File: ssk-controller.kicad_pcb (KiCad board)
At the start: 2 copper layers, 170 x 50 mm, 34 parts, among them J1 Conn_01x16, J2 Conn_01x08, J3 Conn_01x01, J4 USB_B, J5 Solenoid, J6 Solenoid_Signal, Q1 Q_NMOS_GSD, SW1 SW_Push, U1 ATmega32U4-AU, U2 PRTR5V0U2X, Y1 16Mhz

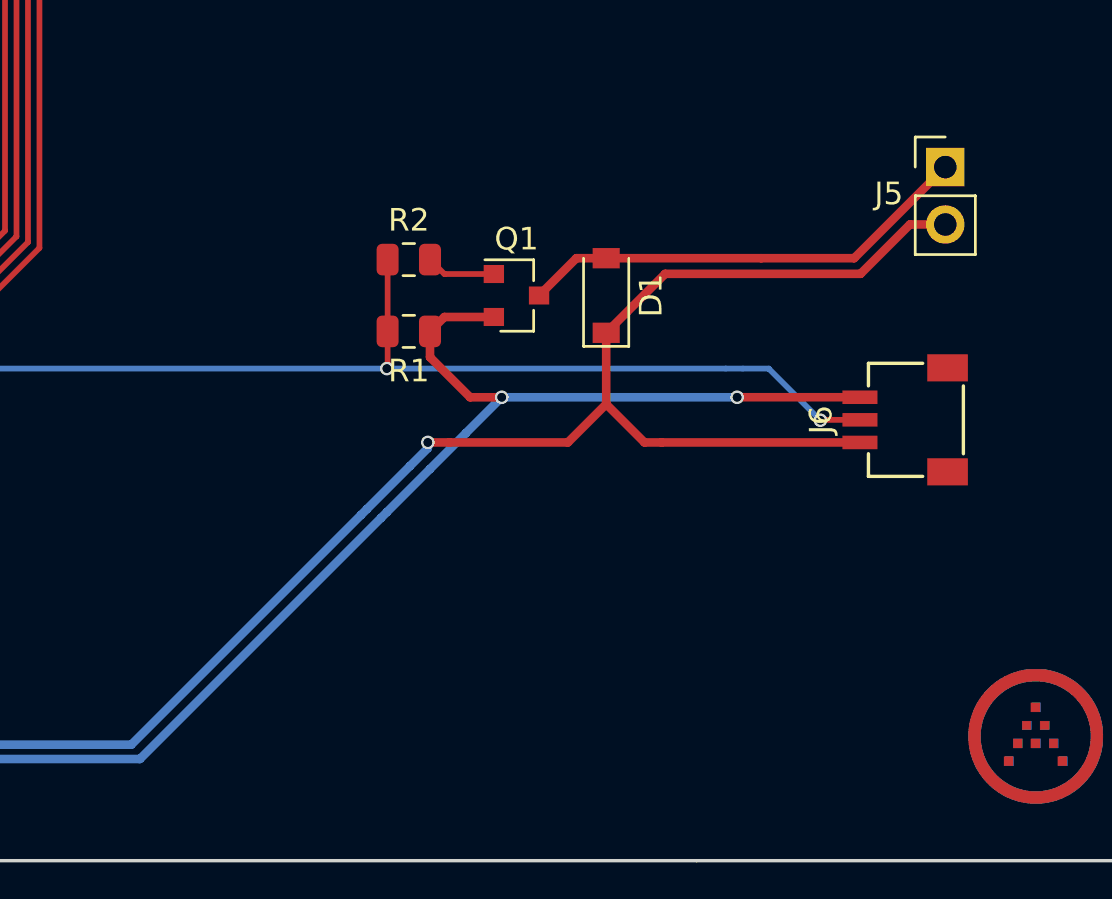
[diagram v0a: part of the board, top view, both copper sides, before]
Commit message: Remove JST header, focus on 5V direct solenoid
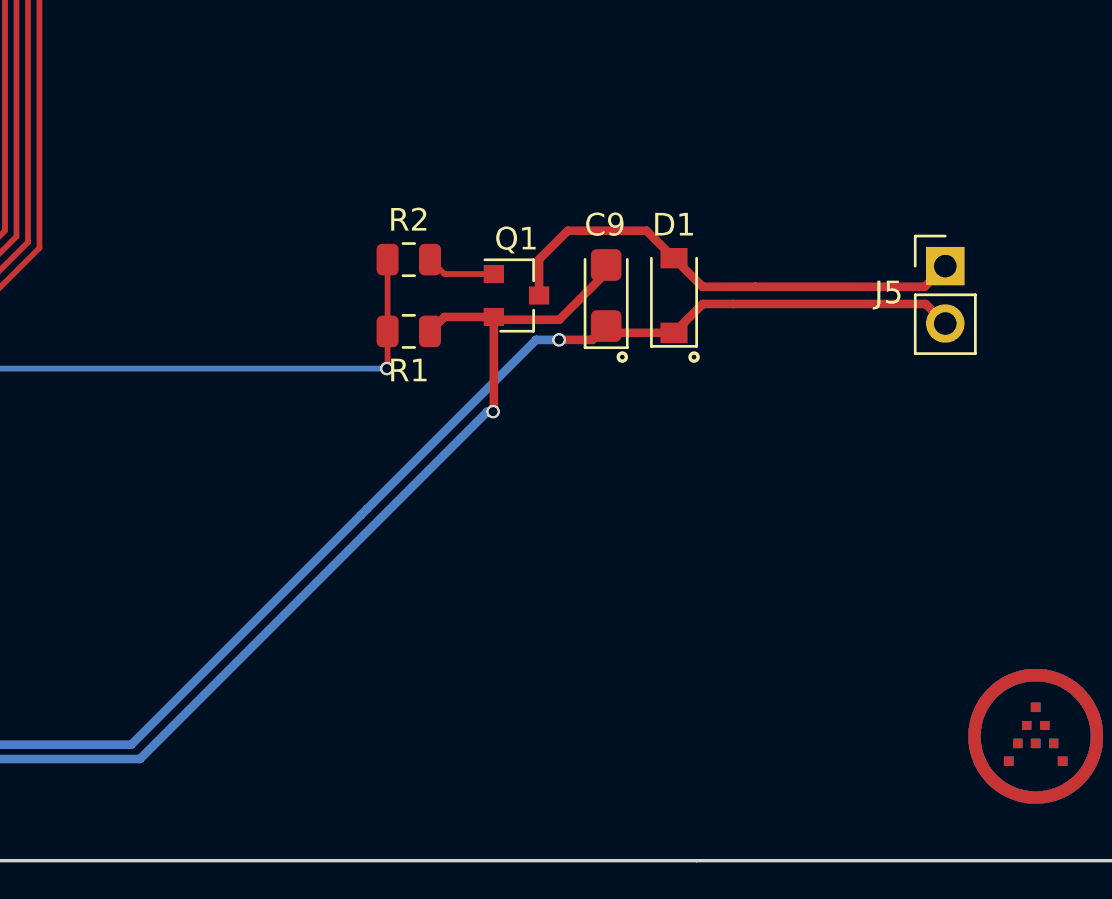
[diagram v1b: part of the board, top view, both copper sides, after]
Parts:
- removed J6: Solenoid_Signal, random-keyboard-parts:JST-SR-3
- added C9: 1uF, Capacitor_Tantalum_SMD:CP_EIA-3216-18_Kemet-A, F.Cu at (235.0, 75.0)
- R1: value 1M -> 10k
- moved J5 4.38 mm to (250.0, 73.7)
- moved D1 3.00 mm to (238.0, 75.0)
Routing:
- net SOLENOID: track 120.9 -> 99.0 mm, vias 3 -> 2
- net +5V: track 280.1 -> 265.3 mm
- net GND: track 301.0 -> 289.9 mm, vias 3 -> 2
- net Net-(D1-Pad2): track 20.3 -> 21.5 mm
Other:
- board text added: "5V Solenoid"
- board text added: "Rev 2.2 20200929"
- board text removed: "5V Solenoid Direct"
- board text removed: "JST SR 3-Pin for Unified Daughterboard S9"
- board text removed: "Rev 2.1 20200331"
